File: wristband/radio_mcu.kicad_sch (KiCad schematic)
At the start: 7 parts, among them U3 NINA-B111, U4 DWM3000

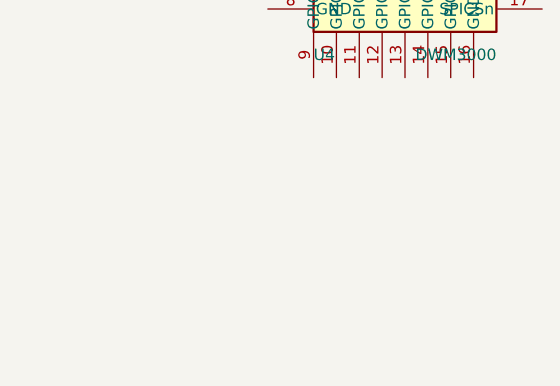
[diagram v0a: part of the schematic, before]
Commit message: Add regulation/antenna/programming-debug sheets; fix confirmed voltage-safety gap
Real datasheet check found a genuine hardware bug in progress, not just a
missing part: NINA-B111 abs-max VCC is 3.9V, DWM3000 abs-max VDD3V3 is
4.0V, but a fully-charged LiPo hits 4.2V -- both boards were about to feed
these ICs straight off the unregulated battery/system rail. Fixed via a
new dedicated regulation sheet per board (placement-only, not wired yet,
same as everything else at this stage):

- wristband/regulation.kicad_sch: MCP1700T-3302E/TT LDO (3.3V, low-Iq),
  current budget verified (NINA-B111 ~12mA + DWM3000 ~55mA vs 250mA
  rating, ~3.7x headroom)
- bay-station/regulation.kicad_sch: TPS62A02PDDCR buck converter (2A,
  single-cell-Li-Ion input range -- the very common TPS563201 was
  considered and rejected, its 4.5V input minimum is incompatible with a
  battery-only rail), current budget verified (ESP32-S3 ~355mA peak +
  4x DWM3000 ~55mA each vs 2A rating, ~3.5x headroom)

Also added, all confirmed against real datasheets:
- wristband/antenna.kicad_sch: ProAnt InSide-2400 BLE antenna (NINA-B111
  needs an external one per u-blox's approved-antenna list; DWM3000 has
  its own onboard antenna already, confirmed, no antenna sheet needed on
  the bay station)
- GPIO5/6 SPI-mode strapping pull-downs on every DWM3000 instance (both
  boards) -- required per Qorvo's own power-up timing diagrams
- wristband/programming_debug.kicad_sch: SWD header for NINA-B111
- bay-station/programming_debug.kicad_sch: ESP32-S3 boot-strap resistors,
  EN RC delay, BOOT/RESET buttons, native-USB flashing interface

One real inconsistency surfaced and flagged (not fixed) in
docs/decisions.md: the bay station's existing power-input USB-C has no
data pins, so a second, data-capable USB-C had to be added for ESP32-S3
flashing rather than consolidating into one connector -- needs a decision.

docs/decisions.md and README.md updated: new items marked resolved with
full reasoning, new open items ad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
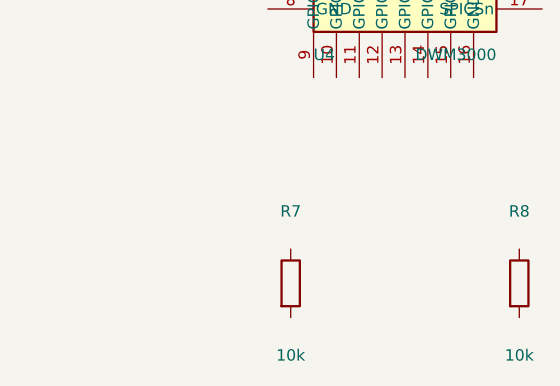
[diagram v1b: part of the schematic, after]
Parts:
- added R7, R8: 10k, Resistor_SMD:R_0603_1608Metric, symbol Device:R
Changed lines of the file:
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@@
+		)
+	)
+	(symbol
+		(lib_id "Device:R")
+		(at 190.5 101.6 0)
+		(unit 1)
+		(exclude_from_sim no)
+		(in_bom yes)
+		(on_board yes)
+		(dnp no)
+		(property "Reference" "R7"
+			(at 190.5 93.6 0)
+			(effects
+				(font
+					(size 1.27 1.27)
+				)
+			)
+		)
+		(property "Value" "10k"
+			(at 190.5 109.6 0)
+			(effects
+				(font
+					(size 1.27 1.27)
+				)
+			)
+		)
+		(property "Footprint" "Resistor_SMD:R_0603_1608Metric"
+			(at 190.5 101.6 0)
+			(effects
+				(font
+					(size 1.27 1.27)
+				)
+				(hide yes)
+			)
+		)
+		(property "Datasheet" ""
+			(at 190.5 101.6 0)
+			(effects
+				(font
+					(size 1.27 1.27)
+				)
+				(hide yes)
+			)
+		)
+		(pin "1"
+		)
+		(pin "2"
+		)
+		(instances
+			(project "wristband"
+				(path "/b3417696-fb19-4c3e-bd30-28bb2d157bef/86c28fe6-4393-4319-af10-ef3feae83fa8"
+					(reference "R7")
+					(unit 1)
+				)
+			)
+		)
+	)
+	(symbol
+		(lib_id "Device:R")
+		(at 215.9 101.6 0)
+		(unit 1)
+		(exclude_from_sim no)
+		(in_bom yes)
+		(on_board yes)
+		(dnp no)
+		(property "Reference" "R8"
+			(at 215.9 93.6 0)
+			(effects
+				(font
+					(size 1.27 1.27)
+				)
+			)
+		)
+		(property "Value" "10k"
+			(at 215.9 109.6 0)
+			(effects
+				(font
+					(size 1.27 1.27)
+				)
+			)
+		)
+		(property "Footprint" "Resistor_SMD:R_0603_1608Metric"
+			(at 215.9 101.6 0)
+			(effects
+				(font
+					(size 1.27 1.27)
+				)
+				(hide yes)
+			)
+		)
+		(property "Datasheet" ""
+			(at 215.9 101.6 0)
+			(effects
+				(font
+					(size 1.27 1.27)
+				)
+				(hide yes)
+			)
+		)
+		(pin "1"
+		)
+		(pin "2"
+		)
+		(instances
+			(project "wristband"
+				(path "/b3417696-fb19-4c3e-bd30-28bb2d157bef/86c28fe6-4393-4319-af10-ef3feae83fa8"
+					(reference "R8")
+					(unit 1)
+				)
+			)
 		)
 	)

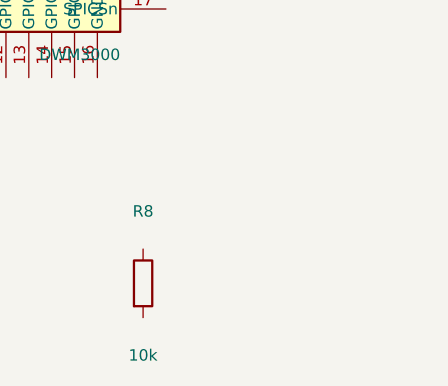
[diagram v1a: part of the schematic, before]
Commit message: Compile passives reference from each chip's real datasheet reference design
New docs/passives-reference.md: per-chip table of every passive called for
by that chip's own real reference/typical-application circuit (not
guessed), cross-referencing what's already placed vs. what the datasheet
actually shows.

Found and fixed one real gap while doing this: Qorvo's own DWM3000
'Example Application Circuit' (Figure 11) shows a 100k pulldown on
IRQ/GPIO8 'to prevent spurious interrupts' -- missing from the design
entirely until now. Added as R9 (wristband/radio_mcu.kicad_sch) and
R25-R28, one per anchor (bay-station/uwb_anchors.kicad_sch).

Also documented two nuances found by reading the same figure closely,
neither of which needed a design change:
- DWM3000's placed decoupling caps go beyond what Qorvo's own minimal
  application circuit shows (the module needs 'only power' per the
  datasheet's own text) -- kept as reasonable conservative practice.
- The GPIO5/6 external strap pull-downs already placed are redundant with
  the chip's own internal default pull-downs (10-30k, varies with VDD1)
  confirmed via the datasheet's GPIO pull-up/down section -- kept
  deliberately for tighter, more deterministic timing margin.

Confirmed via NINA-B1 series datasheet Section 2.1.1: the module has
fully integrated on-board LDO+buck regulation, so needs no external
regulation for its own internal rails (doesn't contradict the external
LDO already added -- that protects the VCC input pin itself from
exceeding its absolute max, a separate concern from internal regulation).

README.md and docs/decisions.md updated to reference the new document and
mark the decoupling-verification 'not done yet' item resolved.
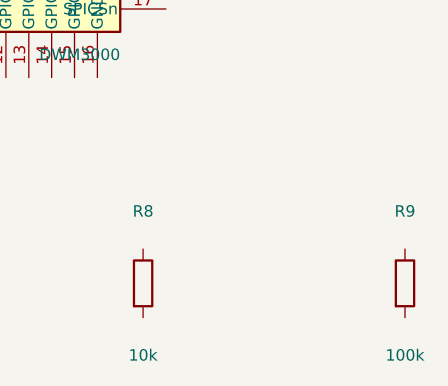
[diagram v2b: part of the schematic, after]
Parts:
- added R9: 100k, Resistor_SMD:R_0603_1608Metric, symbol Device:R
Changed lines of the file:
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@@
+		)
+	)
+	(symbol
+		(lib_id "Device:R")
+		(at 245.0 101.6 0)
+		(unit 1)
+		(exclude_from_sim no)
+		(in_bom yes)
+		(on_board yes)
+		(dnp no)
+		(property "Reference" "R9"
+			(at 245.0 93.6 0)
+			(effects
+				(font
+					(size 1.27 1.27)
+				)
+			)
+		)
+		(property "Value" "100k"
+			(at 245.0 109.6 0)
+			(effects
+				(font
+					(size 1.27 1.27)
+				)
+			)
+		)
+		(property "Footprint" "Resistor_SMD:R_0603_1608Metric"
+			(at 245.0 101.6 0)
+			(effects
+				(font
+					(size 1.27 1.27)
+				)
+				(hide yes)
+			)
+		)
+		(property "Datasheet" ""
+			(at 245.0 101.6 0)
+			(effects
+				(font
+					(size 1.27 1.27)
+				)
+				(hide yes)
+			)
+		)
+		(pin "1"
+		)
+		(pin "2"
+		)
+		(instances
+			(project "wristband"
+				(path "/b3417696-fb19-4c3e-bd30-28bb2d157bef/86c28fe6-4393-4319-af10-ef3feae83fa8"
+					(reference "R9")
+					(unit 1)
+				)
+			)
 		)
 	)
